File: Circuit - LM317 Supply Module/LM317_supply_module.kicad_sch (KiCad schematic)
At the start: 26 parts, among them J1 Conn_01x02, J2 Conn_01x02, J3 Conn_01x02, J4 Conn_01x02, Q1 DMP4011SPSQ, Q2 2N7002, SW1 SW_SPDT, U1 LM317_SOT-223

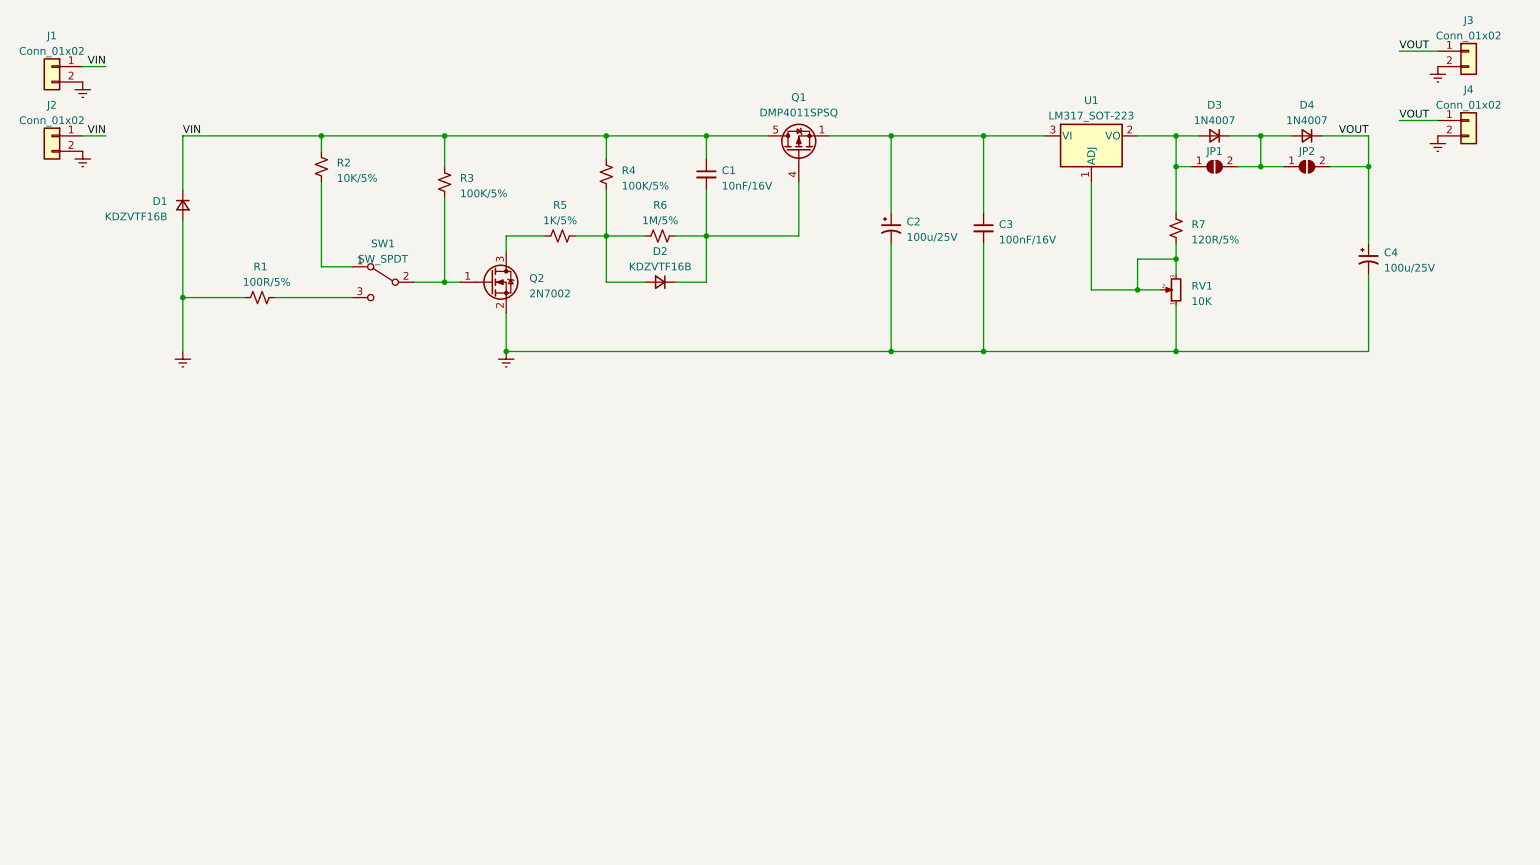
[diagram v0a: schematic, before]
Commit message: update all component footprint
add license CC BY-SA file, update readme
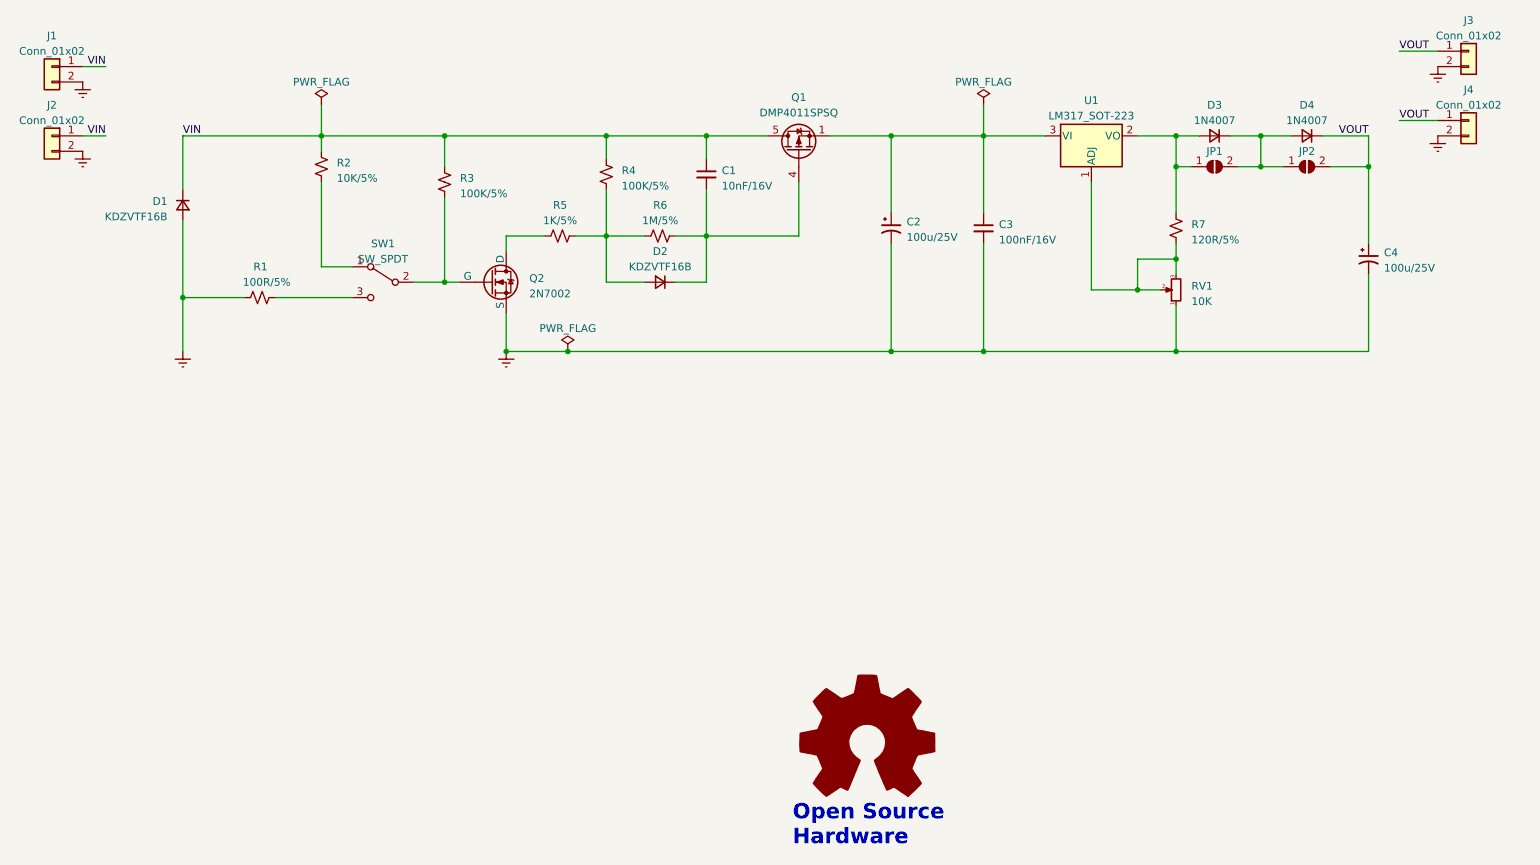
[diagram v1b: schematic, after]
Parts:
- removed Q2: 2N7002, Package_TO_SOT_SMD:SOT-23, symbol Transistor_FET:2N7002
- added Q2: 2N7002, Package_TO_SOT_SMD:SOT-23, symbol Simulation_SPICE:NMOS
- C1, C2, C3, C4: footprint (none) -> Capacitor_SMD:C_0603_1608Metric
- D1, D2: footprint (none) -> Diode_SMD:D_SOD-123F
- D3, D4: footprint (none) -> Diode_SMD:D_SMA
- J1, J2, J3, J4: footprint (none) -> Connector_Phoenix_MC:PhoenixContact_MC_1,5_2-G-3.81_1x02_P3.81mm_Horizontal
- JP1, JP2: footprint (none) -> Jumper:SolderJumper-2_P1.3mm_Open_TrianglePad1.0x1.5mm
- Q1: footprint Package_SON:Diodes_PowerDI3333-8 -> Supply-Module-Library:Diodes_PowerDI5060-8
- R1, R2, R3, R4, R5, R6, R7, RV1: footprint (none) -> Resistor_SMD:R_0603_1608Metric
- SW1: footprint (none) -> Supply-Module-Library:Diodes_PowerDI5060-8
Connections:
- net Earth: now also Q2.3 (S)
- net at R3.2, SW1.2 (B): now also Q2.2 (G)
- net at R5.1: now also Q2.1 (D)
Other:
- note added: "Open Source Hardware"
- title: (none) -> LM317 Supply Module

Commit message: update PCB Layout
update schematic power LED, PCB 3D module file, etc..
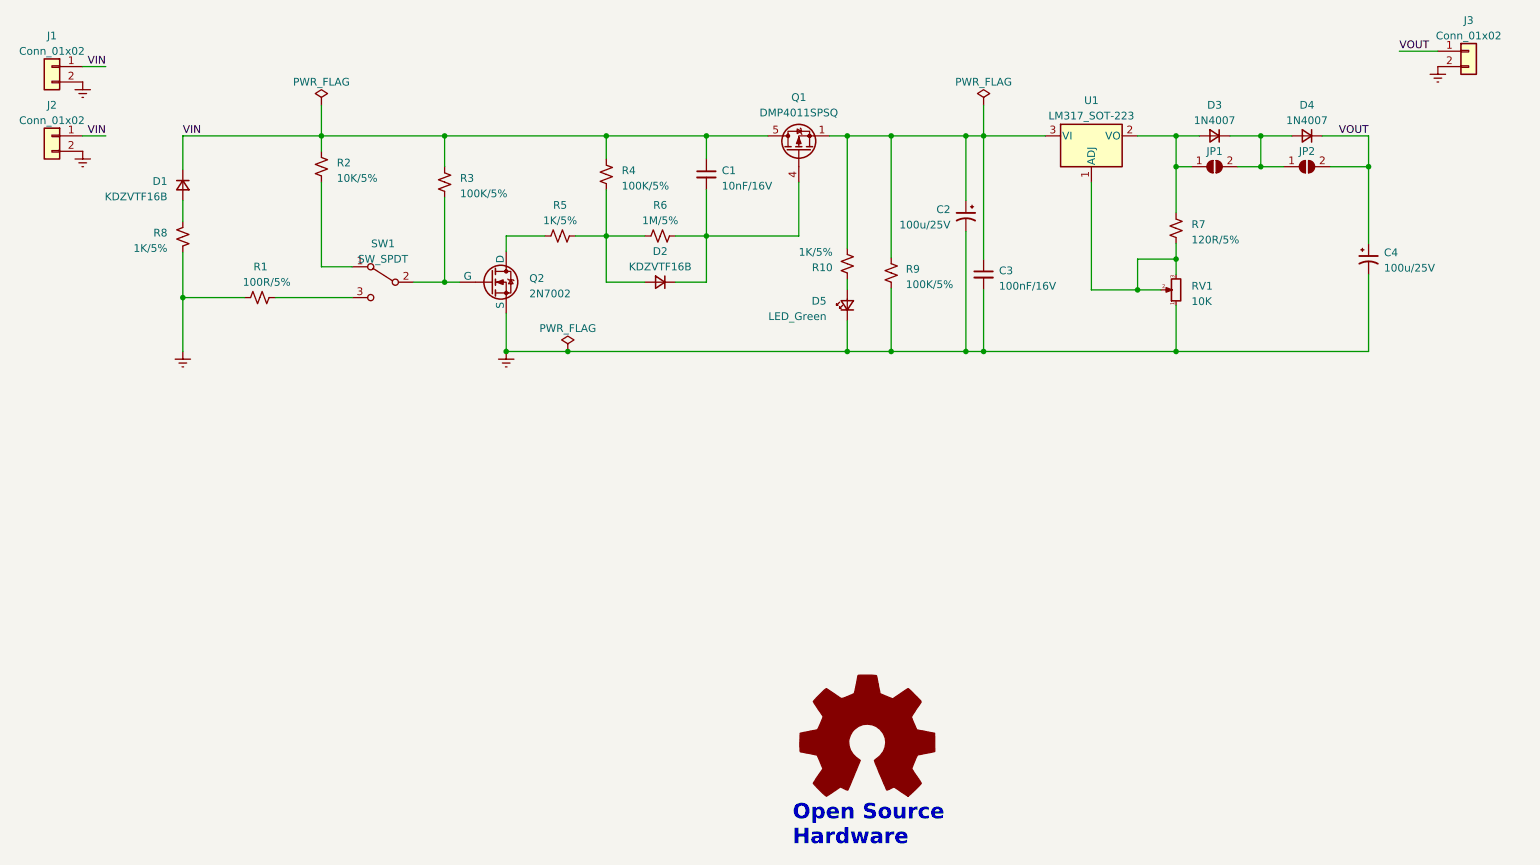
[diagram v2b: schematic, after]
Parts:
- removed J4: Conn_01x02, Connector_Phoenix_MC:PhoenixContact_MC_1,5_2-G-3.81_1x02_P3.81mm_Horizontal, symbol Connector_Generic:Conn_01x02
- added D5: LED_Green, LED_SMD:LED_0603_1608Metric, symbol Device:LED_Small
- added R10, R8: 1K/5%, Resistor_SMD:R_0603_1608Metric, symbol Device:R_Small_US
- added R9: 100K/5%, Resistor_SMD:R_0603_1608Metric, symbol Device:R_Small_US
- C2: footprint Capacitor_SMD:C_0603_1608Metric -> Capacitor_Tantalum_SMD:CP_EIA-7343-30_AVX-N
- RV1: footprint Resistor_SMD:R_0603_1608Metric -> Supply-Module-Library:Variable_Resistance_PV36W
- SW1: footprint Supply-Module-Library:Diodes_PowerDI5060-8 -> Supply-Module-Library:SW_DIP_5176_SPDT
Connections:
- net Earth: now also D5.1 (K), R8.1, R9.2; no longer D1.2 (A)
- net at C2.1, C3.1, Q1.1 (S)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: now also R10.2, R9.1
- new net: D1.2 (A), R8.2
- new net: D5.2 (A), R10.1
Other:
- moved on the sheet: C2, C3, D1

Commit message: PCB Layout Done, DRC OK
update PCB layout, <NEED> Review Gerber file
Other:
- note added: "hardware"
- note added: "open source"
- note removed: "Open Source Hardware"
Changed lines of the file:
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@@
     )
   )
-  (text "Open Source\nHardware" (at 151.384 194.691 0)
-    (effects (font (size 2.54 2.54) (thickness 0.508) bold (color 132 0 0 1)) (justify left bottom))
+  (text " hardware" (at 151.4856 194.1068 0)
+    (effects (font (face "KiCad Font") (size 2.54 2.54) (thickness 0.508) bold (color 132 0 0 1)) (justify left bottom))
+  )
+  (text "open source" (at 151.13 190.5 0)
+    (effects (font (face "KiCad Font") (size 2.54 2.54) (thickness 0.508) bold (color 132 0 0 1)) (justify left bottom))
   )
   (label "VIN" (at 50.8 77.47 0) (fields_autoplaced)
@@
     )
   )
-  (symbol (lib_id "Graphic:Logo_Open_Hardware_Large") (at 163.703 177.673 0) (unit 1)
+  (symbol (lib_id "Graphic:Logo_Open_Hardware_Large") (at 162.56 177.8 0) (unit 1)
     (in_bom no) (on_board no) (dnp no) (fields_autoplaced)
-    (property "Reference" "#SYM1" (at 163.703 164.973 0)
+    (property "Reference" "#SYM1" (at 162.56 165.1 0)
       (effects (font (size 1.27 1.27)) hide)
     )
-    (property "Value" "Logo_Open_Hardware_Large" (at 163.703 187.833 0)
+    (property "Value" "Logo_Open_Hardware_Large" (at 162.56 187.96 0)
       (effects (font (size 1.27 1.27)) hide)
     )
-    (property "Footprint" "" (at 163.703 177.673 0)
+    (property "Footprint" "" (at 162.56 177.8 0)
       (effects (font (size 1.27 1.27)) hide)
     )
-    (property "Datasheet" "~" (at 163.703 177.673 0)
+    (property "Datasheet" "~" (at 162.56 177.8 0)
       (effects (font (size 1.27 1.27)) hide)
     )
-    (property "Sim.Enable" "0" (at 163.703 177.673 0)
+    (property "Sim.Enable" "0" (at 162.56 177.8 0)
       (effects (font (size 1.27 1.27)) hide)
     )

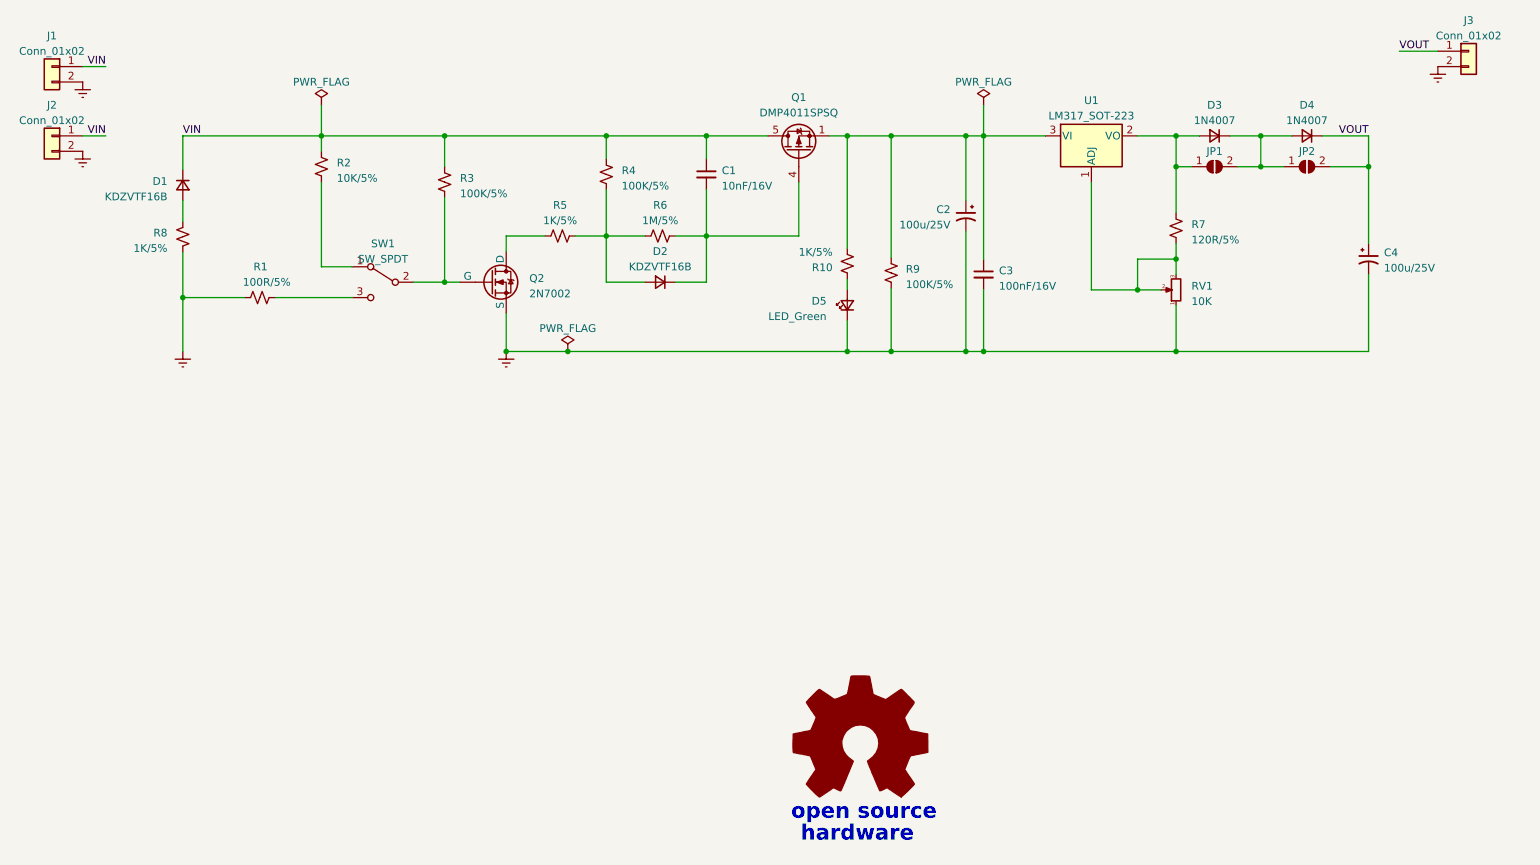
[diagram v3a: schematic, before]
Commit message: Modify Single Layer PCB
modify input/output connector & LED size
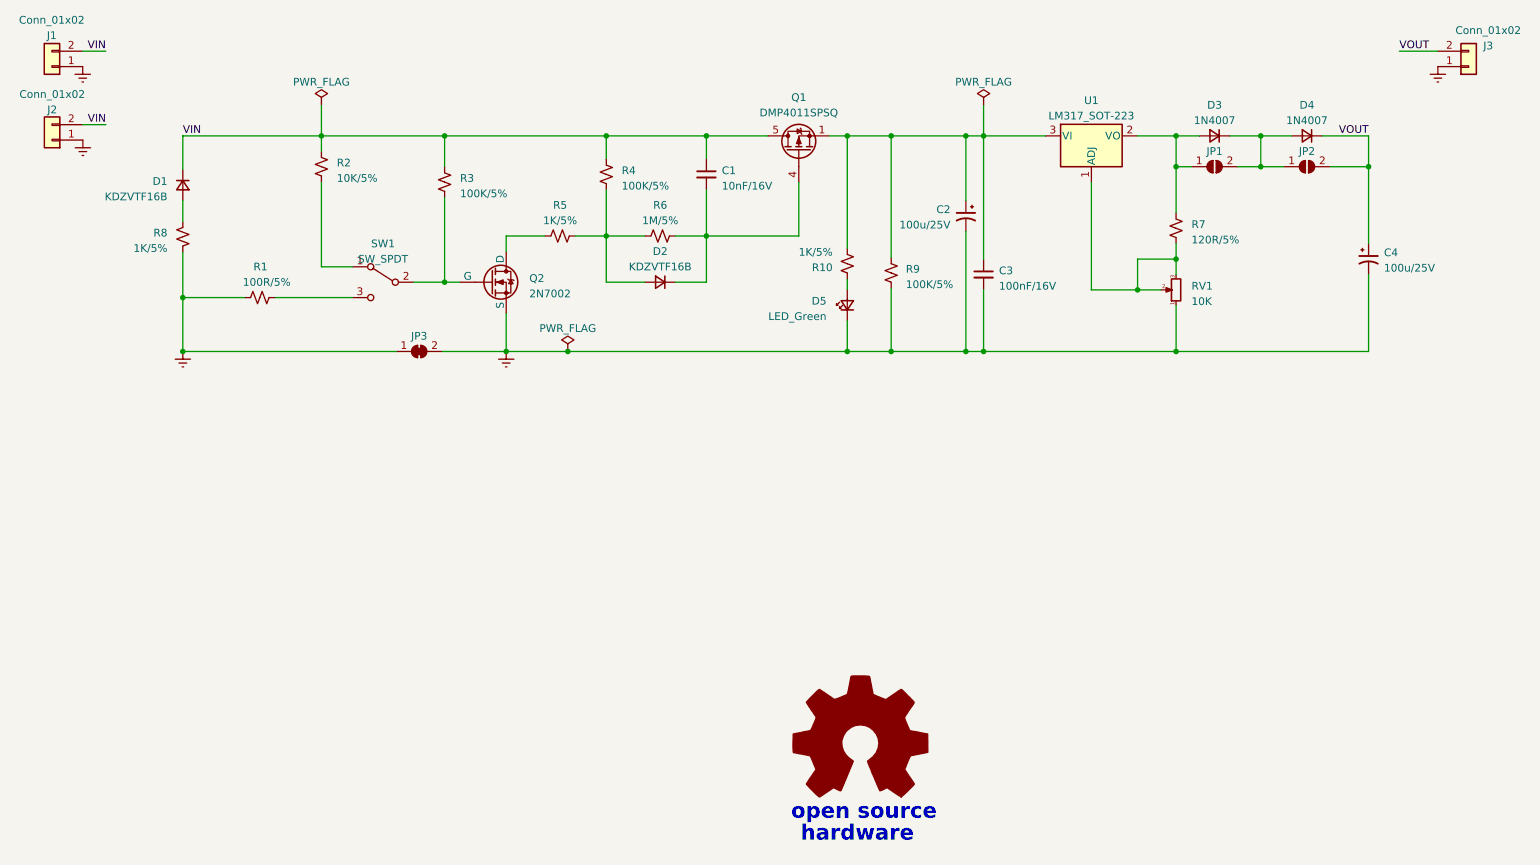
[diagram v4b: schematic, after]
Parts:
- added JP3: SolderJumper_2_Bridged, Jumper:SolderJumper-2_P1.3mm_Bridged_RoundedPad1.0x1.5mm, symbol Jumper:SolderJumper_2_Bridged
- D5: footprint LED_SMD:LED_0603_1608Metric -> LED_SMD:LED_1206_3216Metric
- J2, J3: footprint Connector_Phoenix_MC:PhoenixContact_MC_1,5_2-G-3.81_1x02_P3.81mm_Horizontal -> Connector_Molex:Molex_KK-254_AE-6410-02A_1x02_P2.54mm_Vertical
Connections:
- net Earth: now also J1.1 (Pin_1), J2.1 (Pin_1), JP3.1 (A); no longer C2.2, C3.2, C4.2, D5.1 (K), J1.2 (Pin_2), J2.2 (Pin_2), J3.2 (Pin_2), Q2.3 (S), R9.2, RV1.1
- net VIN: now also J1.2 (Pin_2), J2.2 (Pin_2); no longer J1.1 (Pin_1), J2.1 (Pin_1)
- net VOUT: now also J3.2 (Pin_2); no longer J3.1 (Pin_1)
- new net GNDREF: C2.2, C3.2, C4.2, D5.1 (K), J3.1 (Pin_1), JP3.2 (B), Q2.3 (S), R9.2, RV1.1
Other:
- moved on the sheet: J1, J2
